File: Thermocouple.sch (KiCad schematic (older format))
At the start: 31 parts, among them P2 CONN_2, P3 CONN_3X2, U10 LMT84, U11 OPA4170, U9 MCP3901

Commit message: Back-annotated footprints into the schematic
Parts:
- C10, C30, C31, C5, C6, C7, C8, C9: footprint (none) -> Capacitors_SMD:c_0805
- L5, P2, R25, R26, R27, R43, R44, R47, R48, R62, R63, R64: footprint (none) -> SMD_Packages:SM0805
- P3: footprint (none) -> Pin_Headers:Pin_Header_Straight_2x03
- R21, R22, R23, R24: footprint (none) -> SMD_Packages:SM1206
- TP10, TP8, TP9: footprint (none) -> BenchBudEE:TestPointTH
- U10: footprint (none) -> SMD_Packages:SOT353
- U11: footprint (none) -> SMD_Packages:SO14E
- U9: footprint (none) -> SMD_Packages:SSOP20
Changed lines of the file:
@@
 F 0 "U11" H 7750 2100 60  0000 C CNN
 F 1 "OPA4170" H 7850 1700 50  0000 C CNN
-F 2 "" H 7700 1900 60  0000 C CNN
+F 2 "SMD_Packages:SO14E" H 7700 1900 60  0001 C CNN
 F 3 "" H 7700 1900 60  0000 C CNN
 	3    7700 1900
@@
 F 0 "U11" H 7750 4450 60  0000 C CNN
 F 1 "OPA4170" H 7850 4050 50  0000 C CNN
-F 2 "" H 7700 4250 60  0000 C CNN
+F 2 "SMD_Packages:SO14E" H 7700 4250 60  0001 C CNN
 F 3 "" H 7700 4250 60  0000 C CNN
 	4    7700 4250
@@
 F 0 "U11" H 5250 3200 60  0000 C CNN
 F 1 "OPA4170" H 5350 2800 50  0000 C CNN
-F 2 "" H 5200 3000 60  0000 C CNN
+F 2 "SMD_Packages:SO14E" H 5200 3000 60  0001 C CNN
 F 3 "" H 5200 3000 60  0000 C CNN
 	1    5200 3000
@@
 F 0 "R25" V 6980 2250 40  0000 C CNN
 F 1 "5K" V 6907 2251 40  0000 C CNN
-F 2 "" V 6830 2250 30  0000 C CNN
+F 2 "SMD_Packages:SM0805" V 6830 2250 30  0001 C CNN
 F 3 "" H 6900 2250 30  0000 C CNN
 	1    6900 2250
@@
 F 0 "R27" V 6980 3900 40  0000 C CNN
 F 1 "5K" V 6907 3901 40  0000 C CNN
-F 2 "" V 6830 3900 30  0000 C CNN
+F 2 "SMD_Packages:SM0805" V 6830 3900 30  0001 C CNN
 F 3 "" H 6900 3900 30  0000 C CNN
 	1    6900 3900
@@
 F 0 "R23" V 6430 1900 40  0000 C CNN
 F 1 "200K" V 6357 1901 40  0000 C CNN
-F 2 "" V 6280 1900 30  0000 C CNN
+F 2 "SMD_Packages:SM1206" V 6280 1900 30  0001 C CNN
 F 3 "" H 6350 1900 30  0000 C CNN
 	1    6350 1900
@@
 F 0 "R21" V 5030 1900 40  0000 C CNN
 F 1 "5K" V 4957 1901 40  0000 C CNN
-F 2 "" V 4880 1900 30  0000 C CNN
+F 2 "SMD_Packages:SM1206" V 4880 1900 30  0001 C CNN
 F 3 "" H 4950 1900 30  0000 C CNN
 	1    4950 1900
@@
 F 0 "R24" V 6430 4250 40  0000 C CNN
 F 1 "200K" V 6357 4251 40  0000 C CNN
-F 2 "" V 6280 4250 30  0000 C CNN
+F 2 "SMD_Packages:SM1206" V 6280 4250 30  0001 C CNN
 F 3 "" H 6350 4250 30  0000 C CNN
 	1    6350 4250
@@
 F 0 "R22" V 5030 4250 40  0000 C CNN
 F 1 "5K" V 4957 4251 40  0000 C CNN
-F 2 "" V 4880 4250 30  0000 C CNN
+F 2 "SMD_Packages:SM1206" V 4880 4250 30  0001 C CNN
 F 3 "" H 4950 4250 30  0000 C CNN
 	1    4950 4250
@@
 F 0 "U9" H 3550 1900 60  0000 C CNN
 F 1 "MCP3901" H 2800 3750 60  0000 C CNN
-F 2 "" H 3800 2650 60  0000 C CNN
+F 2 "SMD_Packages:SSOP20" H 3800 2650 60  0001 C CNN
 F 3 "" H 3800 2650 60  0000 C CNN
 	1    2800 2850
@@
 F 0 "C7" H 4700 3400 40  0000 L CNN
 F 1 "100p" H 4706 3215 40  0000 L CNN
-F 2 "" H 4738 3150 30  0000 C CNN
+F 2 "Capacitors_SMD:c_0805" H 4738 3150 30  0001 C CNN
 F 3 "" H 4700 3300 60  0000 C CNN
 	1    4700 3300
@@
 F 0 "P3" H 9000 2850 50  0000 C CNN
 F 1 "CONN_3X2" V 9000 2650 40  0000 C CNN
-F 2 "" H 9000 2600 60  0000 C CNN
+F 2 "Pin_Headers:Pin_Header_Straight_2x03" H 9000 2600 60  0001 C CNN
 F 3 "" H 9000 2600 60  0000 C CNN
 	1    9000 2600
@@
 F 0 "R26" V 9630 3050 40  0000 C CNN
 F 1 "10" V 9557 3051 40  0000 C CNN
-F 2 "" V 9480 3050 30  0000 C CNN
+F 2 "SMD_Packages:SM0805" V 9480 3050 30  0001 C CNN
 F 3 "" H 9550 3050 30  0000 C CNN
 	1    9550 3050
@@
 F 0 "R43" V 9880 3050 40  0000 C CNN
 F 1 "100" V 9807 3051 40  0000 C CNN
-F 2 "" V 9730 3050 30  0000 C CNN
+F 2 "SMD_Packages:SM0805" V 9730 3050 30  0001 C CNN
 F 3 "" H 9800 3050 30  0000 C CNN
 	1    9800 3050
@@
 F 0 "R44" V 10130 3050 40  0000 C CNN
 F 1 "1K" V 10057 3051 40  0000 C CNN
-F 2 "" V 9980 3050 30  0000 C CNN
+F 2 "SMD_Packages:SM0805" V 9980 3050 30  0001 C CNN
 F 3 "" H 10050 3050 30  0000 C CNN
 	1    10050 3050
@@
 F 0 "U10" H 6550 5150 60  0000 C CNN
 F 1 "LMT84" H 6500 5600 60  0000 C CNN
-F 2 "" H 6300 5600 60  0000 C CNN
+F 2 "SMD_Packages:SOT353" H 6300 5600 60  0001 C CNN
 F 3 "" H 6300 5600 60  0000 C CNN
 	1    6300 5600
@@
 F 0 "C10" H 6950 5650 40  0000 L CNN
 F 1 "1u" H 6956 5465 40  0000 L CNN
-F 2 "" H 6988 5400 30  0000 C CNN
+F 2 "Capacitors_SMD:c_0805" H 6988 5400 30  0001 C CNN
 F 3 "" H 6950 5550 60  0000 C CNN
 	1    6950 5550
@@
 F 0 "C8" H 5050 2550 40  0000 L CNN
 F 1 "1u" H 5056 2365 40  0000 L CNN
-F 2 "" H 5088 2300 30  0000 C CNN
+F 2 "Capacitors_SMD:c_0805" H 5088 2300 30  0001 C CNN
 F 3 "" H 5050 2450 60  0000 C CNN
 	1    5050 2450
@@
 F 0 "C9" H 5050 3600 40  0000 L CNN
 F 1 "1u" H 5056 3415 40  0000 L CNN
-F 2 "" H 5088 3350 30  0000 C CNN
+F 2 "Capacitors_SMD:c_0805" H 5088 3350 30  0001 C CNN
 F 3 "" H 5050 3500 60  0000 C CNN
 	1    5050 3500
@@
 F 0 "C6" H 3350 1750 40  0000 L CNN
 F 1 "1u" H 3356 1565 40  0000 L CNN
-F 2 "" H 3388 1500 30  0000 C CNN
+F 2 "Capacitors_SMD:c_0805" H 3388 1500 30  0001 C CNN
 F 3 "" H 3350 1650 60  0000 C CNN
 	1    3350 1650
@@
 F 0 "C5" H 2250 1750 40  0000 L CNN
 F 1 "1u" H 2256 1565 40  0000 L CNN
-F 2 "" H 2288 1500 30  0000 C CNN
+F 2 "Capacitors_SMD:c_0805" H 2288 1500 30  0001 C CNN
 F 3 "" H 2250 1650 60  0000 C CNN
 	1    2250 1650
@@
 F 0 "R48" V 4580 3950 40  0000 C CNN
 F 1 "0" V 4507 3951 40  0000 C CNN
-F 2 "" V 4430 3950 30  0000 C CNN
+F 2 "SMD_Packages:SM0805" V 4430 3950 30  0001 C CNN
 F 3 "" H 4500 3950 30  0000 C CNN
 	1    4500 3950
@@
 F 0 "R47" V 4280 5950 40  0000 C CNN
 F 1 "0" V 4207 5951 40  0000 C CNN
-F 2 "" V 4130 5950 30  0000 C CNN
+F 2 "SMD_Packages:SM0805" V 4130 5950 30  0001 C CNN
 F 3 "" H 4200 5950 30  0000 C CNN
 	1    4200 5950
@@
 F 0 "L5" V 2750 1650 40  0000 C CNN
 F 1 "1u" V 2900 1650 40  0000 C CNN
-F 2 "" H 2800 1650 60  0000 C CNN
+F 2 "SMD_Packages:SM0805" H 2800 1650 60  0001 C CNN
 F 3 "" H 2800 1650 60  0000 C CNN
 	1    2800 1650
@@
 F 0 "C30" H 1500 2400 40  0000 L CNN
 F 1 "NOPOP" H 1506 2215 40  0000 L CNN
-F 2 "" H 1538 2150 30  0000 C CNN
+F 2 "Capacitors_SMD:c_0805" H 1538 2150 30  0001 C CNN
 F 3 "" H 1500 2300 60  0000 C CNN
 	1    1500 2300
@@
 F 0 "C31" H 4150 2400 40  0000 L CNN
 F 1 "NOPOP" H 4156 2215 40  0000 L CNN
-F 2 "" H 4188 2150 30  0000 C CNN
+F 2 "Capacitors_SMD:c_0805" H 4188 2150 30  0001 C CNN
 F 3 "" H 4150 2300 60  0000 C CNN
 	1    4150 2300
@@
 F 0 "P2" V 850 3350 40  0000 C CNN
 F 1 "CONN_2" V 950 3350 40  0000 C CNN
-F 2 "" H 900 3350 60  0000 C CNN
+F 2 "SMD_Packages:SM0805" H 900 3350 60  0001 C CNN
 F 3 "" H 900 3350 60  0000 C CNN
 	1    900  3350
@@
 F 0 "TP10" H 4780 1700 40  0000 L CNN
 F 1 "CH0+" H 4700 1755 30  0001 C CNN
-F 2 "" H 4700 1700 60  0000 C CNN
+F 2 "BenchBudEE:TestPointTH" H 4700 1700 60  0001 C CNN
 F 3 "" H 4700 1700 60  0000 C CNN
 	1    4700 1700
@@
 F 0 "TP9" H 4180 3250 40  0000 L CNN
 F 1 "CH1+" H 4100 3305 30  0001 C CNN
-F 2 "" H 4100 3250 60  0000 C CNN
+F 2 "BenchBudEE:TestPointTH" H 4100 3250 60  0001 C CNN
 F 3 "" H 4100 3250 60  0000 C CNN
 	1    4100 3250
@@
 F 0 "TP8" H 3480 1350 40  0000 L CNN
 F 1 "+5V" H 3400 1405 30  0001 C CNN
-F 2 "" H 3400 1350 60  0000 C CNN
+F 2 "BenchBudEE:TestPointTH" H 3400 1350 60  0001 C CNN
 F 3 "" H 3400 1350 60  0000 C CNN
 	1    3400 1350
@@
 F 0 "R63" V 4580 4550 40  0000 C CNN
 F 1 "0" V 4507 4551 40  0000 C CNN
-F 2 "" V 4430 4550 30  0000 C CNN
+F 2 "SMD_Packages:SM0805" V 4430 4550 30  0001 C CNN
 F 3 "" H 4500 4550 30  0000 C CNN
 	1    4500 4550
@@
 F 0 "R64" V 4880 5600 40  0000 C CNN
 F 1 "1K" V 4807 5601 40  0000 C CNN
-F 2 "" V 4730 5600 30  0000 C CNN
+F 2 "SMD_Packages:SM0805" V 4730 5600 30  0001 C CNN
 F 3 "" H 4800 5600 30  0000 C CNN
 	1    4800 5600
@@
 F 0 "R62" V 4530 5950 40  0000 C CNN
 F 1 "1K" V 4457 5951 40  0000 C CNN
-F 2 "" V 4380 5950 30  0000 C CNN
+F 2 "SMD_Packages:SM0805" V 4380 5950 30  0001 C CNN
 F 3 "" H 4450 5950 30  0000 C CNN
 	1    4450 5950

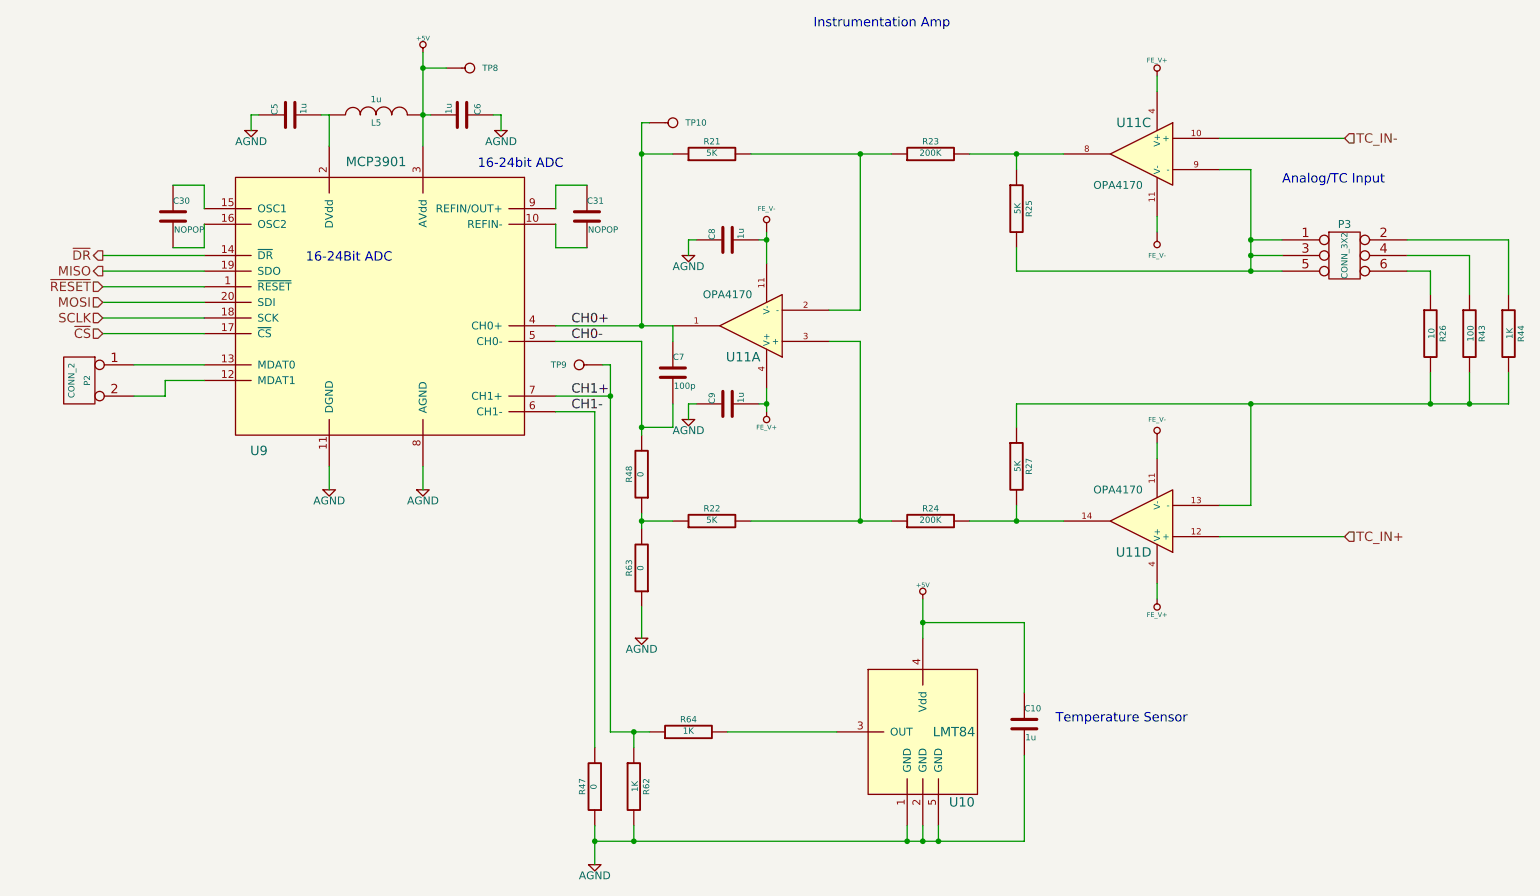
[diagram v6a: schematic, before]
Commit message: Final part numbers added to schematic, cross-checked KiCAD BOM against manual BOM
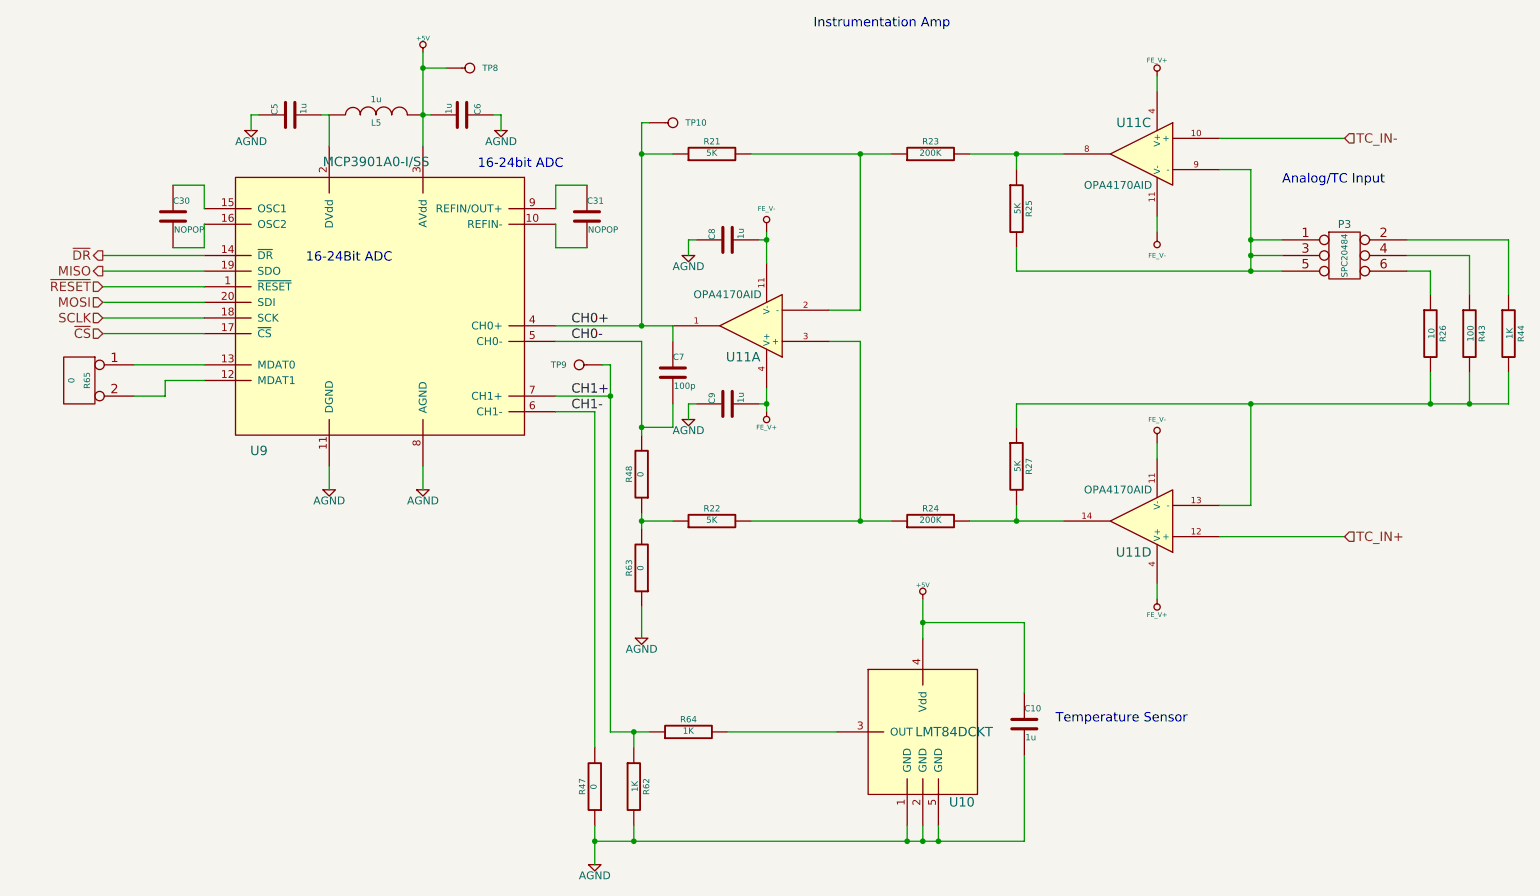
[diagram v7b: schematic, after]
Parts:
- P3: value CONN_3X2 -> SPC20484
- R65: renamed from P2; value CONN_2 -> 0
- U10: value LMT84 -> LMT84DCKT
- U11: value OPA4170 -> OPA4170AID
- U9: value MCP3901 -> MCP3901A0-I/SS
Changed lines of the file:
@@
 P 7700 1900
 F 0 "U11" H 7750 2100 60  0000 C CNN
-F 1 "OPA4170" H 7850 1700 50  0000 C CNN
+F 1 "OPA4170AID" H 7850 1700 50  0000 C CNN
 F 2 "SMD_Packages:SO14E" H 7700 1900 60  0001 C CNN
 F 3 "" H 7700 1900 60  0000 C CNN
@@
 P 7700 4250
 F 0 "U11" H 7750 4450 60  0000 C CNN
-F 1 "OPA4170" H 7850 4050 50  0000 C CNN
+F 1 "OPA4170AID" H 7850 4050 50  0000 C CNN
 F 2 "SMD_Packages:SO14E" H 7700 4250 60  0001 C CNN
 F 3 "" H 7700 4250 60  0000 C CNN
@@
 P 5200 3000
 F 0 "U11" H 5250 3200 60  0000 C CNN
-F 1 "OPA4170" H 5350 2800 50  0000 C CNN
+F 1 "OPA4170AID" H 5350 2800 50  0000 C CNN
 F 2 "SMD_Packages:SO14E" H 5200 3000 60  0001 C CNN
 F 3 "" H 5200 3000 60  0000 C CNN
@@
 P 2800 2850
 F 0 "U9" H 3550 1900 60  0000 C CNN
-F 1 "MCP3901" H 2800 3750 60  0000 C CNN
+F 1 "MCP3901A0-I/SS" H 2800 3750 60  0000 C CNN
 F 2 "SMD_Packages:SSOP20" H 3800 2650 60  0001 C CNN
 F 3 "" H 3800 2650 60  0000 C CNN
@@
 P 9000 2600
 F 0 "P3" H 9000 2850 50  0000 C CNN
-F 1 "CONN_3X2" V 9000 2650 40  0000 C CNN
+F 1 "SPC20484" V 9000 2650 40  0000 C CNN
 F 2 "Pin_Headers:Pin_Header_Straight_2x03" H 9000 2600 60  0001 C CNN
 F 3 "" H 9000 2600 60  0000 C CNN
@@
 P 6300 5600
 F 0 "U10" H 6550 5150 60  0000 C CNN
-F 1 "LMT84" H 6500 5600 60  0000 C CNN
+F 1 "LMT84DCKT" H 6500 5600 60  0000 C CNN
 F 2 "SMD_Packages:SOT353" H 6300 5600 60  0001 C CNN
 F 3 "" H 6300 5600 60  0000 C CNN
@@
 $EndComp
 $Comp
-L FE_V- #PWR63
+L FE_V- #PWR62
 U 1 1 530BD604
 P 5300 2400
-F 0 "#PWR63" H 5300 2600 40  0001 C CNN
+F 0 "#PWR62" H 5300 2600 40  0001 C CNN
 F 1 "FE_V-" H 5300 2550 30  0000 C CNN
 F 2 "" H 5300 2400 60  0000 C CNN
@@
 $EndComp
 $Comp
-L FE_V- #PWR67
+L FE_V- #PWR66
 U 1 1 530BD640
 P 7800 2400
-F 0 "#PWR67" H 7800 2600 40  0001 C CNN
+F 0 "#PWR66" H 7800 2600 40  0001 C CNN
 F 1 "FE_V-" H 7800 2550 30  0000 C CNN
 F 2 "" H 7800 2400 60  0000 C CNN
@@
 $EndComp
 $Comp
-L FE_V- #PWR68
+L FE_V- #PWR67
 U 1 1 530BD64B
 P 7800 3750
-F 0 "#PWR68" H 7800 3950 40  0001 C CNN
+F 0 "#PWR67" H 7800 3950 40  0001 C CNN
 F 1 "FE_V-" H 7800 3900 30  0000 C CNN
 F 2 "" H 7800 3750 60  0000 C CNN
@@
 $EndComp
 $Comp
-L CONN_2 P2
+L CONN_2 R65
 U 1 1 5305902E
 P 900 3350
-F 0 "P2" V 850 3350 40  0000 C CNN
-F 1 "CONN_2" V 950 3350 40  0000 C CNN
+F 0 "R65" V 850 3350 40  0000 C CNN
+F 1 "0" V 950 3350 40  0000 C CNN
 F 2 "SMD_Packages:SM0805" H 900 3350 60  0001 C CNN
 F 3 "" H 900 3350 60  0000 C CNN
